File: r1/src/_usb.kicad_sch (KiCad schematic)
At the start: 14 parts, among them J2 USB-C-12, J3 USB-A-10mm-flangeless, U3 CP2102N-A01-GQFN24

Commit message: Assign MPN's and LCSC part numbers
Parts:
- D5, D6, D7: LCSC (none) -> C261278
- J2: LCSC (none) -> C283540; MPN (none) -> TYPE-C-31-M-17
- U3: LCSC (none) -> C80225; MPN (none) -> CP2102N-A01-GQFN24
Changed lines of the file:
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@@
+      (effects (font (size 1.27 1.27)) hide)
+    )
+    (property "LCSC" "C261278" (at 95.25 87.63 0)
       (effects (font (size 1.27 1.27)) hide)
     )
@@
       (effects (font (size 1.27 1.27)) hide)
     )
+    (property "LCSC" "C261278" (at 104.14 87.63 0)
+      (effects (font (size 1.27 1.27)) hide)
+    )
     (pin "1")
     (pin "2")
@@
       (effects (font (size 1.27 1.27)) hide)
     )
+    (property "LCSC" "C261278" (at 113.03 87.63 0)
+      (effects (font (size 1.27 1.27)) hide)
+    )
     (pin "1")
     (pin "2")
@@
     )
     (property "Datasheet" "" (at 69.85 59.69 0)
+      (effects (font (size 1.27 1.27)) hide)
+    )
+    (property "MPN" "TYPE-C-31-M-17" (at 69.85 59.69 0)
+      (effects (font (size 1.27 1.27)) hide)
+    )
+    (property "LCSC" "C283540" (at 69.85 59.69 0)
       (effects (font (size 1.27 1.27)) hide)
     )
@@
       (effects (font (size 1.27 1.27)) hide)
     )
+    (property "MPN" "CP2102N-A01-GQFN24" (at 175.26 83.82 0)
+      (effects (font (size 1.27 1.27)) hide)
+    )
+    (property "LCSC" "C80225" (at 175.26 83.82 0)
+      (effects (font (size 1.27 1.27)) hide)
+    )

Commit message: Assign manufacturers
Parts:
- J2: Manufacturer (none) -> HRO
- U3: Manufacturer (none) -> Si Labs
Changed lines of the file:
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@@
+      (effects (font (size 1.27 1.27)) hide)
+    )
+    (property "Manufacturer" "HRO" (at 69.85 59.69 0)
       (effects (font (size 1.27 1.27)) hide)
     )
@@
       (effects (font (size 1.27 1.27)) hide)
     )
+    (property "Manufacturer" "Si Labs" (at 175.26 83.82 0)
+      (effects (font (size 1.27 1.27)) hide)
+    )

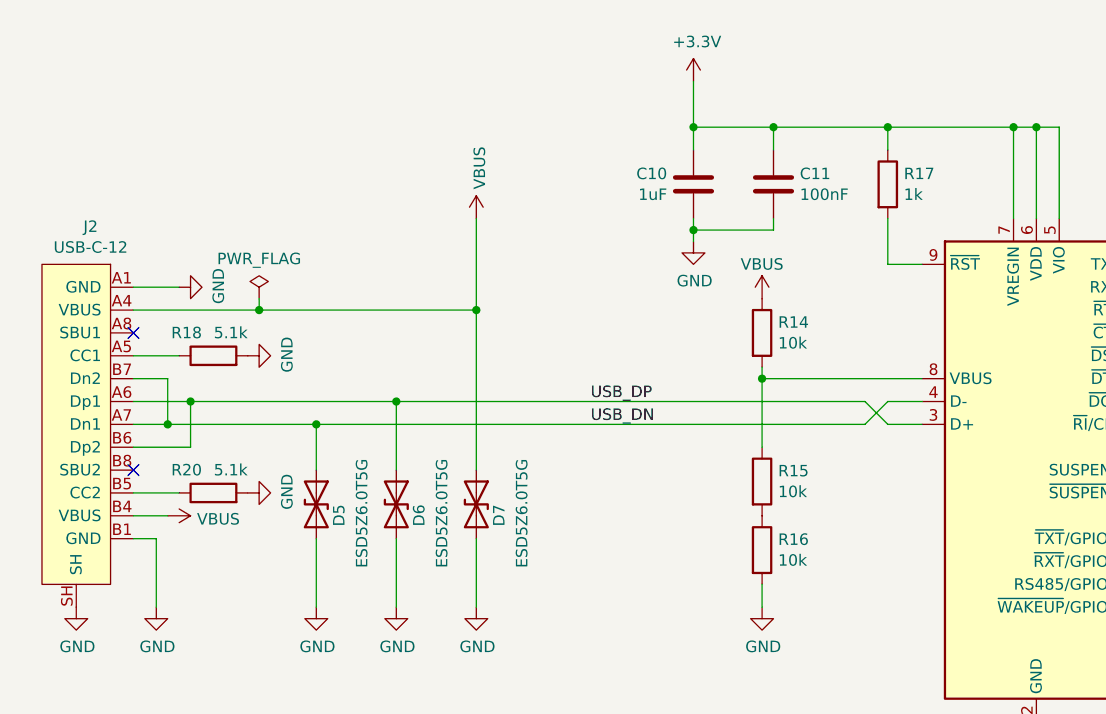
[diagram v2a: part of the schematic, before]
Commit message: Reannotate component refs
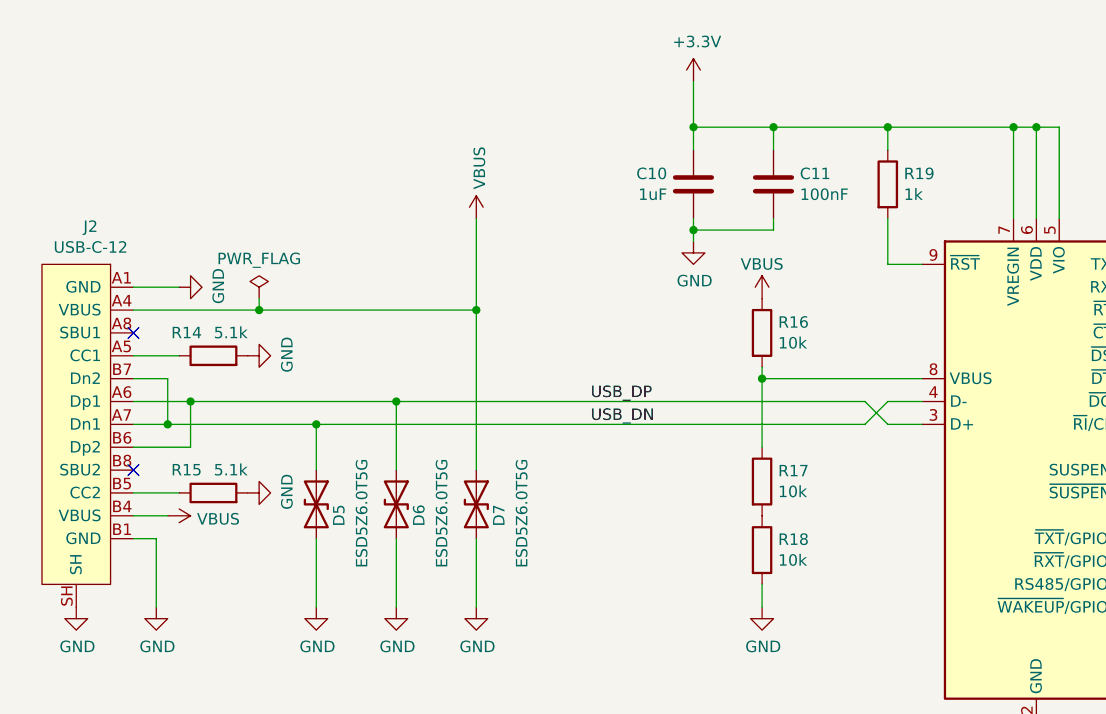
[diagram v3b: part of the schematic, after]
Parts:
- renumbered R18 to R14, R20 to R15, R14 to R16, R15 to R17, R16 to R18, R17 to R19

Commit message: Assign footprints from jeffmakes-footprints lib
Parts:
- D5, D6, D7: footprint jeffmakes-footprints:SOD-523-numbered-pads -> jeffmakes_footprints:SOD-523-numbered-pads
- J2: footprint jeffmakes-footprints:jing-usb-c-lcsc-C167321 -> jeffmakes_footprints:jing-usb-c-lcsc-C167321
- J3: footprint jeffmakes-footprints:USB-A-short-body -> jeffmakes_footprints:USB-A-short-body
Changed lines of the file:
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@@
       (effects (font (size 1.27 1.27)))
     )
-    (property "Footprint" "jeffmakes-footprints:USB-A-short-body" (at 74.93 132.08 0)
+    (property "Footprint" "jeffmakes_footprints:USB-A-short-body" (at 74.93 132.08 0)
       (effects (font (size 1.27 1.27)) (justify left bottom) hide)
     )
@@
       (effects (font (size 1.27 1.27)) (justify left))
     )
-    (property "Footprint" "jeffmakes-footprints:SOD-523-numbered-pads" (at 95.25 87.63 0)
+    (property "Footprint" "jeffmakes_footprints:SOD-523-numbered-pads" (at 95.25 87.63 0)
       (effects (font (size 1.27 1.27)) hide)
     )
@@
       (effects (font (size 1.27 1.27)) (justify left))
     )
-    (property "Footprint" "jeffmakes-footprints:SOD-523-numbered-pads" (at 104.14 87.63 0)
+    (property "Footprint" "jeffmakes_footprints:SOD-523-numbered-pads" (at 104.14 87.63 0)
       (effects (font (size 1.27 1.27)) hide)
     )
@@
       (effects (font (size 1.27 1.27)) (justify left))
     )
-    (property "Footprint" "jeffmakes-footprints:SOD-523-numbered-pads" (at 113.03 87.63 0)
+    (property "Footprint" "jeffmakes_footprints:SOD-523-numbered-pads" (at 113.03 87.63 0)
       (effects (font (size 1.27 1.27)) hide)
     )
@@
       (effects (font (size 1.27 1.27)))
     )
-    (property "Footprint" "jeffmakes-footprints:jing-usb-c-lcsc-C167321" (at 69.85 59.69 0)
-      (effects (font (size 1.27 1.27)) hide)
-    )
+    (property "Footprint" "jeffmakes_footprints:jing-usb-c-lcsc-C167321" (at 69.85 59.69 0)
+      (effects (font (size 1.27 1.27)) hide)
+    )

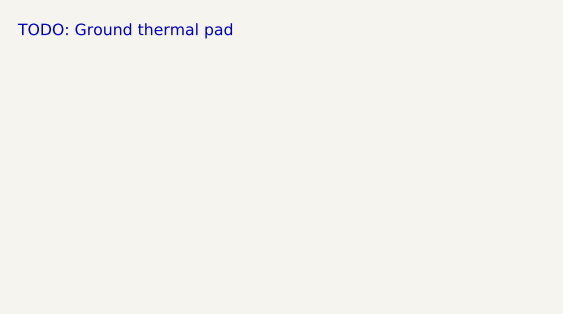
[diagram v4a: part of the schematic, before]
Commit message: ERC pass. Schematic complete.
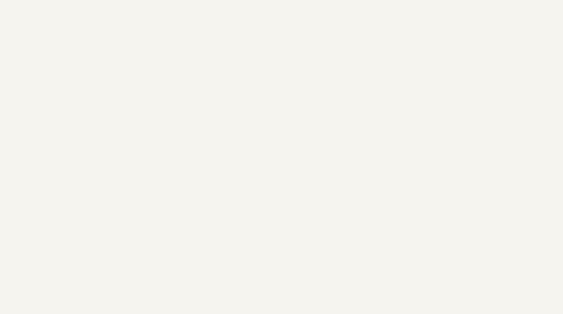
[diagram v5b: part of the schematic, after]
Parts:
- D5, D6, D7: footprint jeffmakes_footprints:SOD-523-numbered-pads -> jeffmakes-footprints:SOD-523-numbered-pads
- J2: footprint jeffmakes_footprints:jing-usb-c-lcsc-C167321 -> jeffmakes-footprints:jing-usb-c-lcsc-C167321
- J3: footprint jeffmakes_footprints:USB-A-short-body -> jeffmakes-footprints:USB-A-short-body
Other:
- note removed: "TODO: Ground thermal pad"
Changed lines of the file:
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@@
     (stroke (width 0) (type default))
-  )
-  (text "TODO: Ground thermal pad" (at 29.21 24.13 0)
-    (effects (font (size 1.27 1.27)) (justify left bottom))
   )
   (label "USB_DP" (at 125.73 76.2 0) (fields_autoplaced)
@@
       (effects (font (size 1.27 1.27)))
     )
-    (property "Footprint" "jeffmakes_footprints:USB-A-short-body" (at 74.93 132.08 0)
+    (property "Footprint" "jeffmakes-footprints:USB-A-short-body" (at 74.93 132.08 0)
       (effects (font (size 1.27 1.27)) (justify left bottom) hide)
     )
@@
       (effects (font (size 1.27 1.27)) (justify left))
     )
-    (property "Footprint" "jeffmakes_footprints:SOD-523-numbered-pads" (at 95.25 87.63 0)
+    (property "Footprint" "jeffmakes-footprints:SOD-523-numbered-pads" (at 95.25 87.63 0)
       (effects (font (size 1.27 1.27)) hide)
     )
@@
       (effects (font (size 1.27 1.27)) (justify left))
     )
-    (property "Footprint" "jeffmakes_footprints:SOD-523-numbered-pads" (at 104.14 87.63 0)
+    (property "Footprint" "jeffmakes-footprints:SOD-523-numbered-pads" (at 104.14 87.63 0)
       (effects (font (size 1.27 1.27)) hide)
     )
@@
       (effects (font (size 1.27 1.27)) (justify left))
     )
-    (property "Footprint" "jeffmakes_footprints:SOD-523-numbered-pads" (at 113.03 87.63 0)
+    (property "Footprint" "jeffmakes-footprints:SOD-523-numbered-pads" (at 113.03 87.63 0)
       (effects (font (size 1.27 1.27)) hide)
     )
@@
       (effects (font (size 1.27 1.27)))
     )
-    (property "Footprint" "jeffmakes_footprints:jing-usb-c-lcsc-C167321" (at 69.85 59.69 0)
-      (effects (font (size 1.27 1.27)) hide)
-    )
+    (property "Footprint" "jeffmakes-footprints:jing-usb-c-lcsc-C167321" (at 69.85 59.69 0)
+      (effects (font (size 1.27 1.27)) hide)
+    )
